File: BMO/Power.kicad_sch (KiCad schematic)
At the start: 44 parts, among them J1 USB_C_Receptacle_USB2.0_16P, J2 Conn_01x03_Pin, Q1 DMP1045U-7, U2 MMDT2907A-7-F, U3 USBLC6-2SC6, U4 BQ27220YZFR, U5 BQ25895RTW, U6 AP2112K-3.3

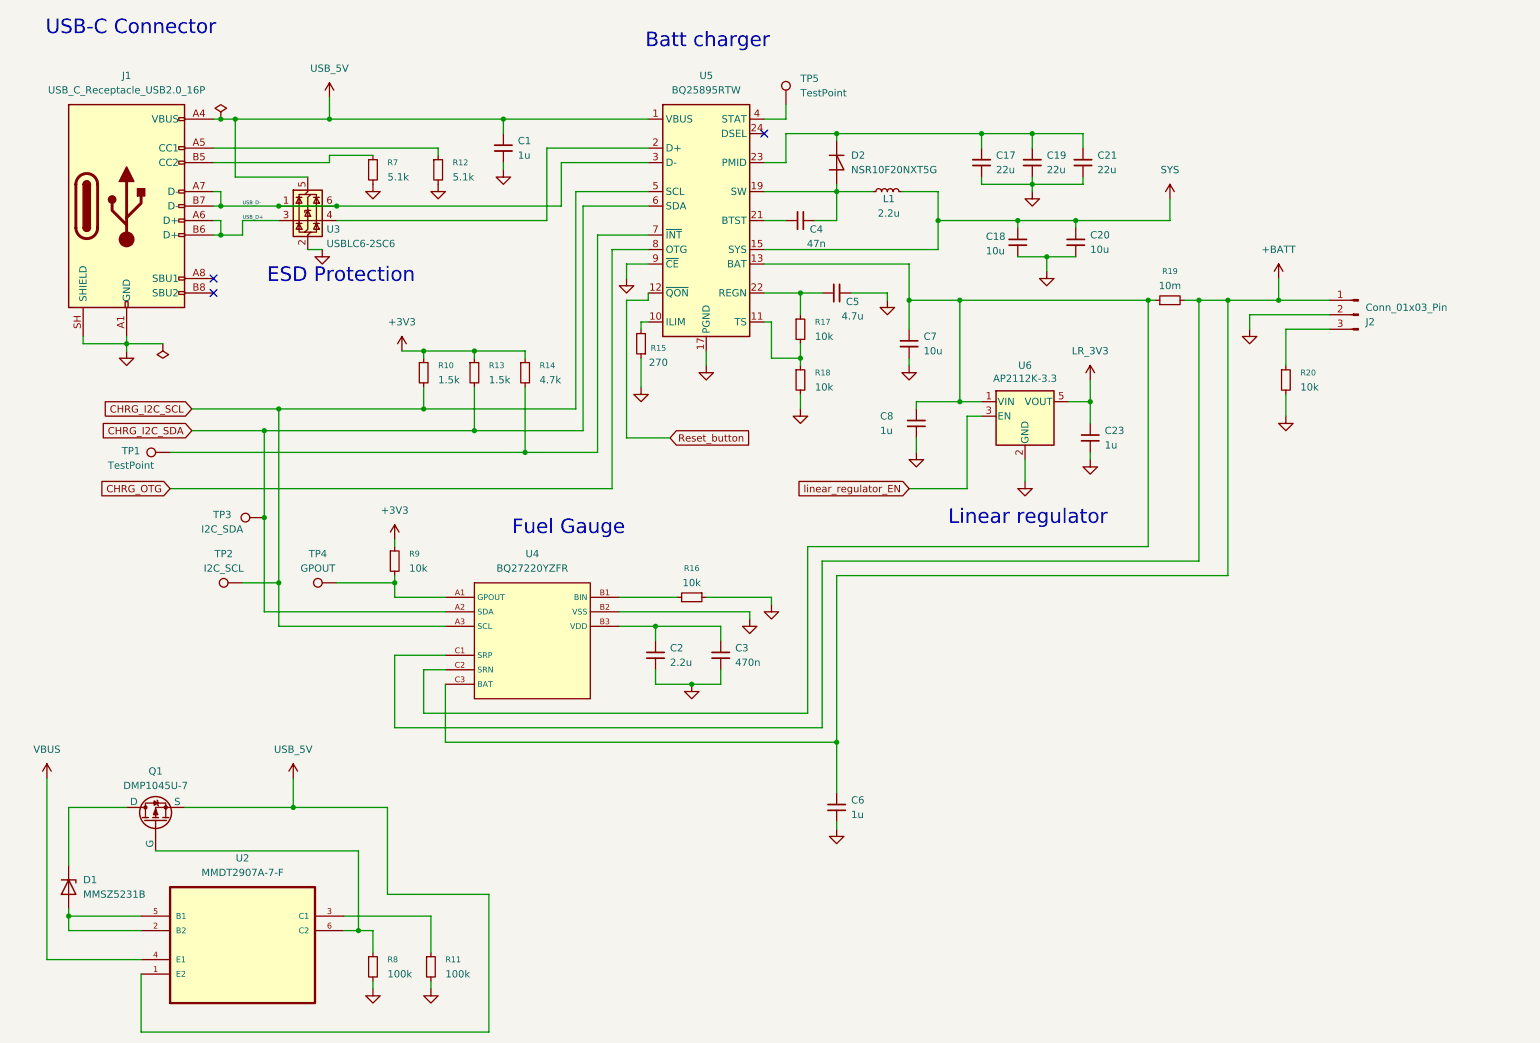
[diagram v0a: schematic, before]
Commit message: Updated Power schematic, Added Motors driver schematic
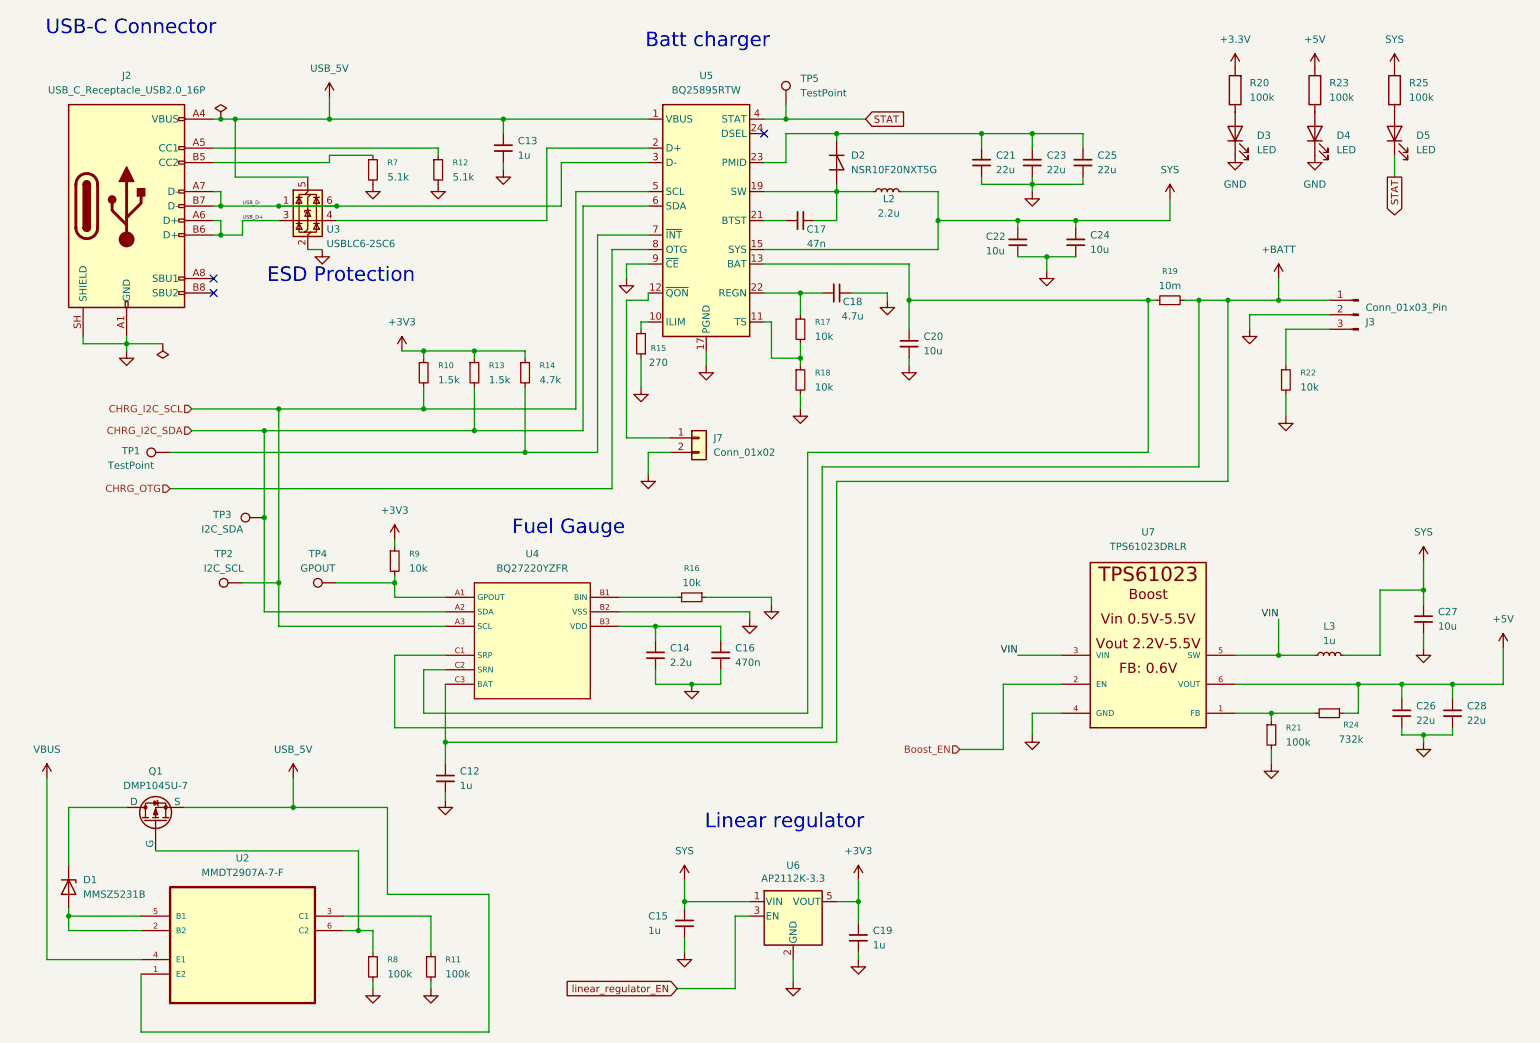
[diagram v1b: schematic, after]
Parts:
- removed C23, C6, C8: 1u, Capacitor_SMD:C_0402_1005Metric, symbol Device:C_Small
- added C12, C15, C19: 1u, Capacitor_SMD:C_0402_1005Metric, symbol Device:C_Small
- added C26, C28: 22u, Capacitor_SMD:C_1210_3225Metric, symbol Device:C_Small
- added C27: 10u, Capacitor_SMD:C_0603_1608Metric, symbol Device:C_Small
- added D3, D4, D5: LED, symbol Kicad:LED
- added J7: Conn_01x02, Connector_JST:JST_GH_SM02B-GHS-TB_1x02-1MP_P1.25mm_Horizontal, symbol Connector_Generic:Conn_01x02
- added L3: 1u, Inductor_SMD:L_0805_2012Metric, symbol Device:L_Small
- added R20, R23, R25: 100k, symbol Kicad:R
- added R21: 100k, Resistor_SMD:R_0603_1608Metric, symbol Device:R_Small
- added R24: 732k, Resistor_SMD:R_0603_1608Metric, symbol Device:R_Small
- added U7: TPS61023DRLR, TPS61023DRLR:SOT563-ORI, symbol jlcpcb_symbol:TPS61023DRLR
- renumbered C1 to C13, C2 to C14, C3 to C16, C4 to C17, C5 to C18, C7 to C20, C17 to C21, C18 to C22, C19 to C23, C20 to C24, C21 to C25, J1 to J2, J2 to J3, L1 to L2, R20 to R22
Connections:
- net LR_3V3 is gone; now on net +3V3: U6.5 (VOUT)
- net +3V3: now also C19.1
- net +BATT: now also C12.1
- net GND: now also C12.2, C15.2, C19.2, C26.2, C27.2, C28.2, D3.1 (K), D4.1 (K), J7.2 (Pin_2), R21.2, U7.4 (GND)
- net SYS: now also U6.1 (VIN), C15.1, C27.1, L3.2, R25.2
- net at C20.1, R19.1, U4.C2 (SRN)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: no longer U6.1 (VIN)
- net STAT: now reaches TP5.1, U5.4 (STAT)
- net STAT: now also D5.1 (K)
- net Reset_button: no longer names the net of U5.12 (~{QON})
- net Reset_button: now also J7.1 (Pin_1)
- new net: R21.1, R24.2, U7.1 (FB)
- new net: D4.2 (A), R23.1
- new net: D5.2 (A), R25.1
- new net: D3.2 (A), R20.1
- new net +3.3V: R20.2
- new net +5V: C26.1, C28.1, R23.2, R24.1, U7.6 (VOUT)
- new net Boost_EN: U7.2 (EN)
- new net VIN: L3.1, U7.3 (VIN), U7.5 (SW)

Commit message: Update sensor and MCU files
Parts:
- removed C12, C13, C15: 1u, Capacitor_SMD:C_0402_1005Metric, symbol Device:C_Small
- removed C14: 2.2u, Capacitor_SMD:C_0603_1608Metric, symbol Device:C_Small
- removed C16: 470n, Capacitor_SMD:C_0603_1608Metric, symbol Device:C_Small
- removed C22: 10u, Capacitor_SMD:C_0402_1005Metric, symbol Device:C_Small
- removed C26, C28: 22u, Capacitor_SMD:C_1210_3225Metric, symbol Device:C_Small
- removed L2: 2.2u, Inductor_SMD:L_0603_1608Metric, symbol Device:L_Small
- added C30, C33, C36, C37, C39: 22u, Capacitor_SMD:C_1210_3225Metric, symbol Device:C_Small
- added C32, C35: 10u, Capacitor_SMD:C_0402_1005Metric, symbol Device:C_Small
- added C38: 10u, Capacitor_SMD:C_0603_1608Metric, symbol Device:C_Small
- added L4: 1u, Inductor_SMD:L_0805_2012Metric, symbol Device:L_Small
- C17: value 47n -> 1u; footprint Capacitor_SMD:C_0603_1608Metric -> Capacitor_SMD:C_0402_1005Metric; JLCPCB Part # C1622 -> C52923
- C18: value 4.7u -> 1u; footprint Capacitor_SMD:C_0603_1608Metric -> Capacitor_SMD:C_0402_1005Metric; JLCPCB Part # C19666 -> C52923
- C19: value 1u -> 2.2u; footprint Capacitor_SMD:C_0402_1005Metric -> Capacitor_SMD:C_0603_1608Metric; JLCPCB Part # C52923 -> C23630
- C20: value 10u -> 1u; footprint Capacitor_SMD:C_0603_1608Metric -> Capacitor_SMD:C_0402_1005Metric; JLCPCB Part # C96446 -> C52923
- C21: value 22u -> 470n; footprint Capacitor_SMD:C_1210_3225Metric -> Capacitor_SMD:C_0603_1608Metric; JLCPCB Part # C52306 -> C1623
- C23: value 22u -> 47n; footprint Capacitor_SMD:C_1210_3225Metric -> Capacitor_SMD:C_0603_1608Metric; JLCPCB Part # C52306 -> C1622
- C24: value 10u -> 4.7u; footprint Capacitor_SMD:C_0402_1005Metric -> Capacitor_SMD:C_0603_1608Metric; JLCPCB Part # C15525 -> C19666
- C25: value 22u -> 1u; footprint Capacitor_SMD:C_1210_3225Metric -> Capacitor_SMD:C_0402_1005Metric; JLCPCB Part # C52306 -> C52923
- L3: value 1u -> 2.2u; footprint Inductor_SMD:L_0805_2012Metric -> Inductor_SMD:L_0603_1608Metric; JLCPCB Part # C19533 -> C1033
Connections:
- net +3V3: now also C25.1; no longer C19.1
- net +5V: now also C37.1, C39.1
- net +BATT: now also C17.1
- net GND: now also C17.2, C18.2, C24.1, C30.2, C32.2, C33.2, C35.2, C36.2, C37.2, C38.2, C39.2; no longer C18.1, C23.2, C24.2
- net SYS: now also C20.1, C32.1, C35.1, C38.1, L4.2; no longer C24.1, C27.1
- net USB_5V: now also C18.1
- net VIN: now also L4.1; no longer L3.1
- net at D2.2 (A), U5.19 (SW), U5.20 (SW): now also C23.1, L3.1; no longer C17.1
- net at U4.B3 (VDD): now also C19.1, C21.1
- net at R17.1, U5.22 (REGN): now also C24.2; no longer C18.2
- net at R19.1, U4.C2 (SRN), U5.13 (BAT)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: now also C27.1; no longer C20.1
- net at U5.21 (BTST): now also C23.2; no longer C17.2
- new net: C30.1, C33.1, C36.1, D2.1 (K), U5.23 (PMID)
